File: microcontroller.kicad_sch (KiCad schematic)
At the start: 1 part, among them U1 ESP32-WROOM-32E

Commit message: Adding ethernet module and more
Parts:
- added C5, C6: 100n, symbol Device:C
- added FB8: 0R, Inductor_SMD:L_0603_1608Metric, symbol Device:FerriteBead
- added Q7: UMH3N, Package_TO_SOT_SMD:SOT-363_SC-70-6, symbol Transistor_BJT:UMH3N
- added R8: 10k, symbol Device:R
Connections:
- net 3V3: now also FB8.1
- net GND: now also C5.2, C6.2
- net at U1.2 (VDD): now also C6.1, FB8.2, R8.1
- net at U1.25 (IO0): now also Q7.3 (C2)
- net at U1.3 (EN): now also C5.1, Q7.6 (C1), R8.2
- net ESP_RXD0: now reaches U1.34 (RXD0/IO3)
- net ESP_TXD0: now reaches U1.35 (TXD0/IO1)
- new net CH_DTR: Q7.2 (B1), Q7.4 (E2)
- new net CH_RTS: Q7.1 (E1), Q7.5 (B2)

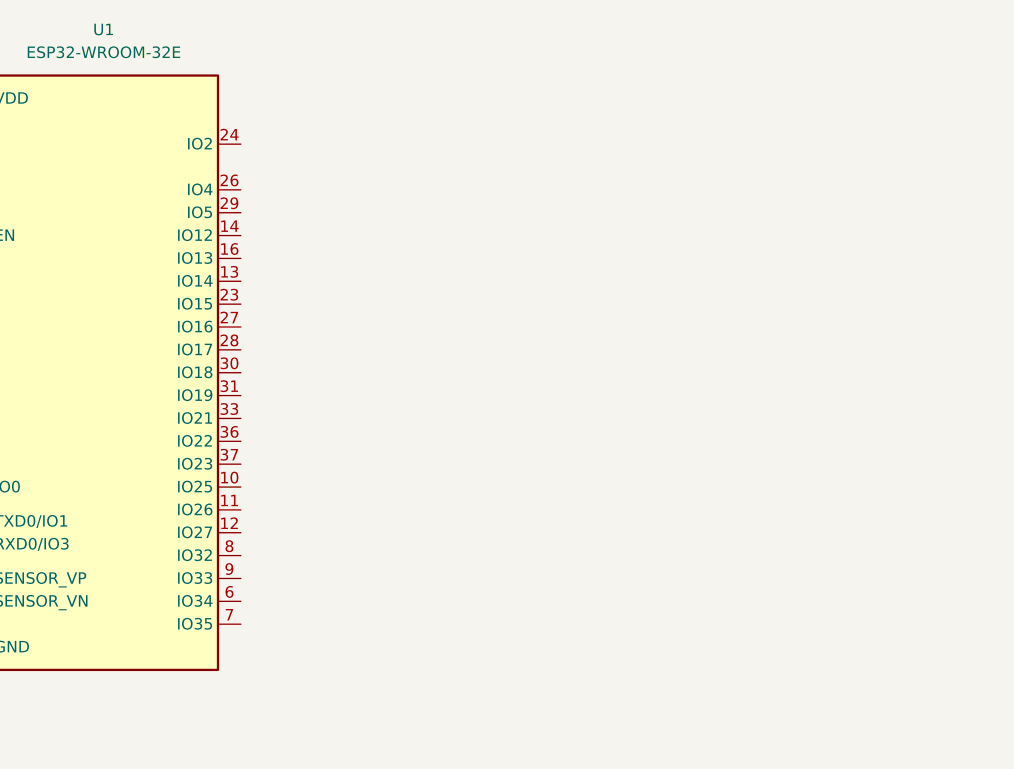
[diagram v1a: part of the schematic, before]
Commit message: Ethernet progress, 40pin connector, save progress
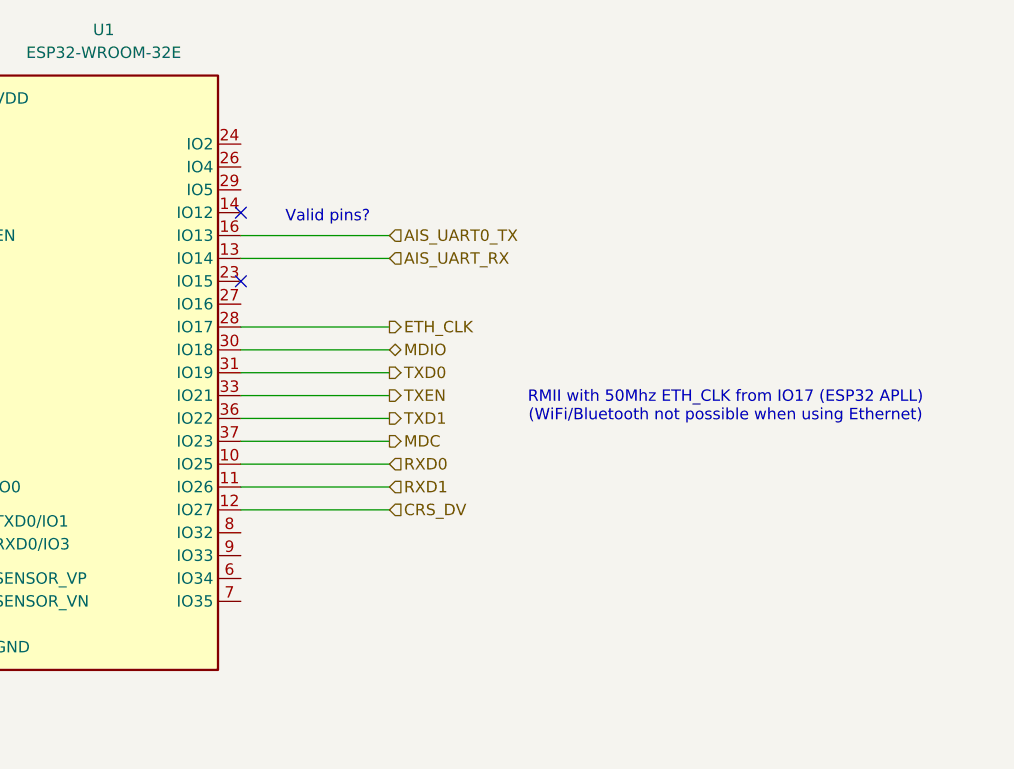
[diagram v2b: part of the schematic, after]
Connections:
- net RXD0: now reaches U1.10 (IO25)
- net RXD1: now reaches U1.11 (IO26)
- net CRS_DV: now reaches U1.12 (IO27)
- net AIS_UART_RX: now reaches U1.13 (IO14)
- net AIS_UART0_TX: now reaches U1.16 (IO13)
- net ETH_CLK: now reaches U1.28 (IO17)
- net MDIO: now reaches U1.30 (IO18)
- net TXD0: now reaches U1.31 (IO19)
- net TXEN: now reaches U1.33 (IO21)
- net TXD1: now reaches U1.36 (IO22)
- net MDC: now reaches U1.37 (IO23)
- no-connect marks 0 -> 2
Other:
- note added: "RMII with 50Mhz ETH_CLK from IO17 (ESP32 APLL) (WiFi/Bluetooth not possible when using Ethernet)"
- note added: "Valid pins?"
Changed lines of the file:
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@@
 	(generator_version "10.0")
 	(paper "A4")
+	(text "RMII with 50Mhz ETH_CLK from IO17 (ESP32 APLL)\n(WiFi/Bluetooth not possible when using Ethernet)"
+		(exclude_from_sim no)
+		(at 215.138 95.25 0)
+		(effects
+			(font
+				(size 1.27 1.27)
+			)
+		)
+	)
+	(text "Valid pins?"
+		(exclude_from_sim no)
+		(at 170.942 74.168 0)
+		(effects
+			(font
+				(size 1.27 1.27)
+			)
+		)
+	)
 	(junction
 		(at 41.91 82.55)
@@
 		(color 0 0 0 0)
 	)
+	(no_connect
+		(at 161.29 73.66)
+	)
+	(no_connect
+		(at 161.29 81.28)
+	)
 	(wire
 		(pts
@@
 	(wire
 		(pts
+			(xy 161.29 99.06) (xy 177.8 99.06)
+		)
+		(stroke
+			(width 0)
+			(type default)
+		)
+	)
+	(wire
+		(pts
 			(xy 80.01 60.96) (xy 34.29 60.96)
 		)
@@
 	(wire
 		(pts
+			(xy 161.29 96.52) (xy 177.8 96.52)
+		)
+		(stroke
+			(width 0)
+			(type default)
+		)
+	)
+	(wire
+		(pts
 			(xy 116.84 81.28) (xy 116.84 76.2)
 		)
@@
 	(wire
 		(pts
+			(xy 161.29 93.98) (xy 177.8 93.98)
+		)
+		(stroke
+			(width 0)
+			(type default)
+		)
+	)
+	(wire
+		(pts
 			(xy 66.04 77.47) (xy 66.04 76.2)
 		)
@@
 	(wire
 		(pts
+			(xy 161.29 101.6) (xy 177.8 101.6)
+		)
+		(stroke
+			(width 0)
+			(type default)
+		)
+	)
+	(wire
+		(pts
+			(xy 161.29 76.2) (xy 177.8 76.2)
+		)
+		(stroke
+			(width 0)
+			(type default)
+		)
+	)
+	(wire
+		(pts
+			(xy 161.29 106.68) (xy 177.8 106.68)
+		)
+		(stroke
+			(width 0)
+			(type default)
+		)
+	)
+	(wire
+		(pts
 			(xy 66.04 88.9) (xy 40.64 88.9)
 		)
@@
 	(wire
 		(pts
+			(xy 161.29 91.44) (xy 177.8 91.44)
+		)
+		(stroke
+			(width 0)
+			(type default)
+		)
+	)
+	(wire
+		(pts
 			(xy 34.29 110.49) (xy 130.81 110.49)
 		)
@@
 	(wire
 		(pts
+			(xy 161.29 78.74) (xy 177.8 78.74)
+		)
+		(stroke
+			(width 0)
+			(type default)
+		)
+	)
+	(wire
+		(pts
 			(xy 66.04 92.71) (xy 66.04 91.44)
 		)
@@
 	(wire
 		(pts
+			(xy 161.29 88.9) (xy 177.8 88.9)
+		)
+		(stroke
+			(width 0)
+			(type default)
+		)
+	)
+	(wire
+		(pts
+			(xy 161.29 104.14) (xy 177.8 104.14)
+		)
+		(stroke
+			(width 0)
+			(type default)
+		)
+	)
+	(wire
+		(pts
 			(xy 34.29 121.92) (xy 123.19 121.92)
 		)
@@
 	(wire
 		(pts
+			(xy 161.29 86.36) (xy 177.8 86.36)
+		)
+		(stroke
+			(width 0)
+			(type default)
+		)
+	)
+	(wire
+		(pts
 			(xy 40.64 97.79) (xy 55.88 97.79)
 		)
@@
 		)
 	)
+	(hierarchical_label "AIS_UART0_TX"
+		(shape input)
+		(at 177.8 76.2 0)
+		(effects
+			(font
+				(size 1.27 1.27)
+			)
+			(justify left)
+		)
+	)
+	(hierarchical_label "AIS_UART_RX"
+		(shape input)
+		(at 177.8 78.74 0)
+		(effects
+			(font
+				(size 1.27 1.27)
+			)
+			(justify left)
+		)
+	)
+	(hierarchical_label "TXD0"
+		(shape output)
+		(at 177.8 91.44 0)
+		(effects
+			(font
+				(size 1.27 1.27)
+			)
+			(justify left)
+		)
+	)
+	(hierarchical_label "ETH_CLK"
+		(shape output)
+		(at 177.8 86.36 0)
+		(effects
+			(font
+				(size 1.27 1.27)
+			)
+			(justify left)
+		)
+	)
 	(hierarchical_label "CH_RTS"
 		(shape output)
@@
 		)
 	)
+	(hierarchical_label "RXD1"
+		(shape input)
+		(at 177.8 104.14 0)
+		(effects
+			(font
+				(size 1.27 1.27)
+			)
+			(justify left)
+		)
+	)
+	(hierarchical_label "CRS_DV"
+		(shape input)
+		(at 177.8 106.68 0)
+		(effects
+			(font
+				(size 1.27 1.27)
+			)
+			(justify left)
+		)
+	)
+	(hierarchical_label "TXD1"
+		(shape output)
+		(at 177.8 96.52 0)
+		(effects
+			(font
+				(size 1.27 1.27)
+			)
+			(justify left)
+		)
+	)
 	(hierarchical_label "ESP_RXD0"
 		(shape input)
@@
 		)
 	)
+	(hierarchical_label "MDIO"
+		(shape bidirectional)
+		(at 177.8 88.9 0)
+		(effects
+			(font
+				(size 1.27 1.27)
+			)
+			(justify left)
+		)
+	)
 	(hierarchical_label "3V3"
 		(shape input)
@@
 		)
 	)
+	(hierarchical_label "TXEN"
+		(shape output)
+		(at 177.8 93.98 0)
+		(effects
+			(font
+				(size 1.27 1.27)
+			)
+			(justify left)
+		)
+	)
 	(hierarchical_label "CH_DTR"
 		(shape input)
@@
 		)
 	)
+	(hierarchical_label "RXD0"
+		(shape input)
+		(at 177.8 101.6 0)
+		(effects
+			(font
+				(size 1.27 1.27)
+			)
+			(justify left)
+		)
+	)
+	(hierarchical_label "MDC"
+		(shape output)
+		(at 177.8 99.06 0)
+		(effects
+			(font
+				(size 1.27 1.27)
+			)
+			(justify left)
+		)
+	)

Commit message: NMEA0183 and NMEA2000 schematics
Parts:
- added R59: 0R, Resistor_SMD:R_0603_1608Metric, symbol Device:R
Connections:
- net at U1.14 (IO12): now also R59.1
- net MODEM_RX: now reaches U1.26 (IO4)
- net MODEM_TX: now reaches U1.27 (IO16)
- net MODEM_DTR: now reaches U1.4 (SENSOR_VP)
- net CAN_TX: now reaches U1.6 (IO34)
- net CAN_RX: now reaches U1.7 (IO35)
- net NMEA0183_TX: now reaches U1.8 (IO32)
- net NMEA0183_RX: now reaches U1.9 (IO33)
- net AIS_UART_RX renamed AIS_UART0_RX
- new net MODEM_PWR: R59.2
- no-connect marks 2 -> 6
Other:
- note added: "Optional for future design"
- note added: "strapping pin"
- note added: "| Pin | Default | Description | | --- | --- | --- | | IO5 | Pull-up | Voltage level of IO5 and IO15 affects the timing of SDIO Slave. | | IO0 | Pull-up | Pull LOW to enter download mode. | | IO2 | Pull-down | IO0 and IO2 together will make ESP32 enter download mode. | | IO12 (MTDI) | Pull-down | Pull HIGH and ESP32 will fail to boot normally. | | IO15 (MTDO) | Pull-up | Pull LOW to disable debug 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"
- note removed: "Valid pins?"

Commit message: Clean up and testpoints
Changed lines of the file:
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@@
 	(text "RMII with 50Mhz ETH_CLK from IO17 (ESP32 APLL)\n(WiFi/Bluetooth not possible when using Ethernet)"
 		(exclude_from_sim no)
-		(at 215.138 95.25 0)
+		(at 216.916 86.614 0)
 		(effects
 			(font

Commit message: Layout save
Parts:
- C5, C6: footprint (none) -> Capacitor_SMD:C_0603_1608Metric
- R8: footprint (none) -> Resistor_SMD:R_0603_1608Metric
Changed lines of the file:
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@@
 			)
 		)
-		(property "Footprint" ""
+		(property "Footprint" "Resistor_SMD:R_0603_1608Metric"
 			(at 115.062 68.58 90)
 			(hide yes)
@@
 			)
 		)
-		(property "Footprint" ""
+		(property "Footprint" "Capacitor_SMD:C_0603_1608Metric"
 			(at 103.8352 88.9 0)
 			(hide yes)
@@
 			)
 		)
-		(property "Footprint" ""
+		(property "Footprint" "Capacitor_SMD:C_0603_1608Metric"
 			(at 117.8052 88.9 0)
 			(hide yes)

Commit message: Power layout started
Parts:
- added C36: 10uF, Capacitor_SMD:C_0603_1608Metric, symbol Device:C
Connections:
- net GND: now also C36.2
- net at C6.1, FB8.2, R8.1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: now also C36.1
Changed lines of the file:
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@@
+	)
+	(junction
+		(at 90.17 60.96)
+		(diameter 0)
+		(color 0 0 0 0)
 	)
 	(junction
@@
 	(wire
 		(pts
+			(xy 90.17 81.28) (xy 90.17 60.96)
+		)
+		(stroke
+			(width 0)
+			(type default)
+		)
+	)
+	(wire
+		(pts
 			(xy 161.29 114.3) (xy 177.8 114.3)
 		)
@@
 	(wire
 		(pts
+			(xy 90.17 88.9) (xy 90.17 92.71)
+		)
+		(stroke
+			(width 0)
+			(type default)
+		)
+	)
+	(wire
+		(pts
 			(xy 116.84 76.2) (xy 130.81 76.2)
 		)
@@
 	(wire
 		(pts
+			(xy 90.17 60.96) (xy 102.87 60.96)
+		)
+		(stroke
+			(width 0)
+			(type default)
+		)
+	)
+	(wire
+		(pts
 			(xy 34.29 121.92) (xy 123.19 121.92)
 		)
@@
 	(wire
 		(pts
-			(xy 102.87 60.96) (xy 87.63 60.96)
+			(xy 87.63 60.96) (xy 90.17 60.96)
 		)
 		(stroke
@@
 	)
 	(symbol
+		(lib_id "power:GND")
+		(at 90.17 92.71 0)
+		(unit 1)
+		(body_style 1)
+		(exclude_from_sim no)
+		(in_bom yes)
+		(on_board yes)
+		(in_pos_files yes)
+		(dnp no)
+		(fields_autoplaced yes)
+		(property "Reference" "#PWR076"
+			(at 90.17 99.06 0)
+			(hide yes)
+			(show_name no)
+			(do_not_autoplace no)
+			(effects
+				(font
+					(size 1.27 1.27)
+				)
+			)
+		)
+		(property "Value" "GND"
+			(at 90.17 97.79 0)
+			(show_name no)
+			(do_not_autoplace no)
+			(effects
+				(font
+					(size 1.27 1.27)
+				)
+			)
+		)
+		(property "Footprint" ""
+			(at 90.17 92.71 0)
+			(hide yes)
+			(show_name no)
+			(do_not_autoplace no)
+			(effects
+				(font
+					(size 1.27 1.27)
+				)
+			)
+		)
+		(property "Datasheet" ""
+			(at 90.17 92.71 0)
+			(hide yes)
+			(show_name no)
+			(do_not_autoplace no)
+			(effects
+				(font
+					(size 1.27 1.27)
+				)
+			)
+		)
+		(property "Description" "Power symbol creates a global label with name \"GND\" , ground"
+			(at 90.17 92.71 0)
+			(hide yes)
+			(show_name no)
+			(do_not_autoplace no)
+			(effects
+				(font
+					(size 1.27 1.27)
+				)
+			)
+		)
+		(pin "1"
+		)
+		(instances
+			(project "AIS-Converter"
+				(path "/af2e2bda-c8b0-494b-9cbc-4303d4ae7608/f7b96531-3096-4981-b0a1-7516608a6c61"
+					(reference "#PWR076")
+					(unit 1)
+				)
+			)
+		)
+	)
+	(symbol
 		(lib_id "Device:C")
 		(at 116.84 85.09 0)
@@
 					(unit 1)
 				)
+			)
+		)
+	)
+	(symbol
+		(lib_id "Device:C")
+		(at 90.17 85.09 0)
+		(unit 1)
+		(body_style 1)
+		(exclude_from_sim no)
+		(in_bom yes)
+		(on_board yes)
+		(in_pos_files yes)
+		(dnp no)
+		(fields_autoplaced yes)
+		(property "Reference" "C36"
+			(at 93.98 83.8199 0)
+			(show_name no)
+			(do_not_autoplace no)
+			(effects
+				(font
+					(size 1.27 1.27)
+				)
+				(justify left)
+			)
+		)
+		(property "Value" "10uF"
+			(at 93.98 86.3599 0)
+			(show_name no)
+			(do_not_autoplace no)
+			(effects
+				(font
+					(size 1.27 1.27)
+				)
+				(justify left)
+			)
+		)
+		(property "Footprint" "Capacitor_SMD:C_0603_1608Metric"
+			(at 91.1352 88.9 0)
+			(hide yes)
+			(show_name no)
+			(do_not_autoplace no)
+			(effects
+				(font
+					(size 1.27 1.27)
+				)
+			)
+		)
+		(property "Datasheet" ""
+			(at 90.17 85.09 0)
+			(hide yes)
+			(show_name no)
+			(do_not_autoplace no)
+			(effects
+				(font
+					(size 1.27 1.27)
+				)
+			)
+		)
+		(property "Description" "Unpolarized capacitor"
+			(at 90.17 85.09 0)
+			(hide yes)
+			(show_name no)
+			(do_not_autoplace no)
+			(effects
+				(font
+					(size 1.27 1.27)
+				)
+			)
+		)
+		(pin "1"
+		)
+		(pin "2"
+		)
+		(instances
+			(project "AIS-Converter"
+				(path "/af2e2bda-c8b0-494b-9cbc-4303d4ae7608/f7b96531-3096-4981-b0a1-7516608a6c61"
+					(reference "C36")
+					(unit 1)
+				)
